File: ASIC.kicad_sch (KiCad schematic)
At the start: 69 parts, among them U10 MCP1824T-1202E/OT, U11 MCP1824T-0802E, U12 25MHz, U4 BM1370_mode1, U5 BM1370_mode1, U9 SN74AVC4T774

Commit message: start rough parts placement
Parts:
- R14: footprint (none) -> Resistor_SMD:R_0402_1005Metric; DK (none) -> 311-20.0KLRCT-ND; PARTNO (none) -> RC0402FR-0720KL
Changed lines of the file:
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@@
 			)
 		)
-		(property "Footprint" ""
+		(property "Footprint" "Resistor_SMD:R_0402_1005Metric"
 			(at 172.72 52.07 0)
 			(effects
@@
 			(at 172.72 52.07 0)
 			(effects
+				(font
+					(size 1.27 1.27)
+				)
+				(hide yes)
+			)
+		)
+		(property "PARTNO" "RC0402FR-0720KL"
+			(at 172.72 52.07 0)
+			(effects
+				(font
+					(size 1.27 1.27)
+				)
+				(hide yes)
+			)
+		)
+		(property "DK" "311-20.0KLRCT-ND"
+			(at 172.72 52.07 0)
+			(effects

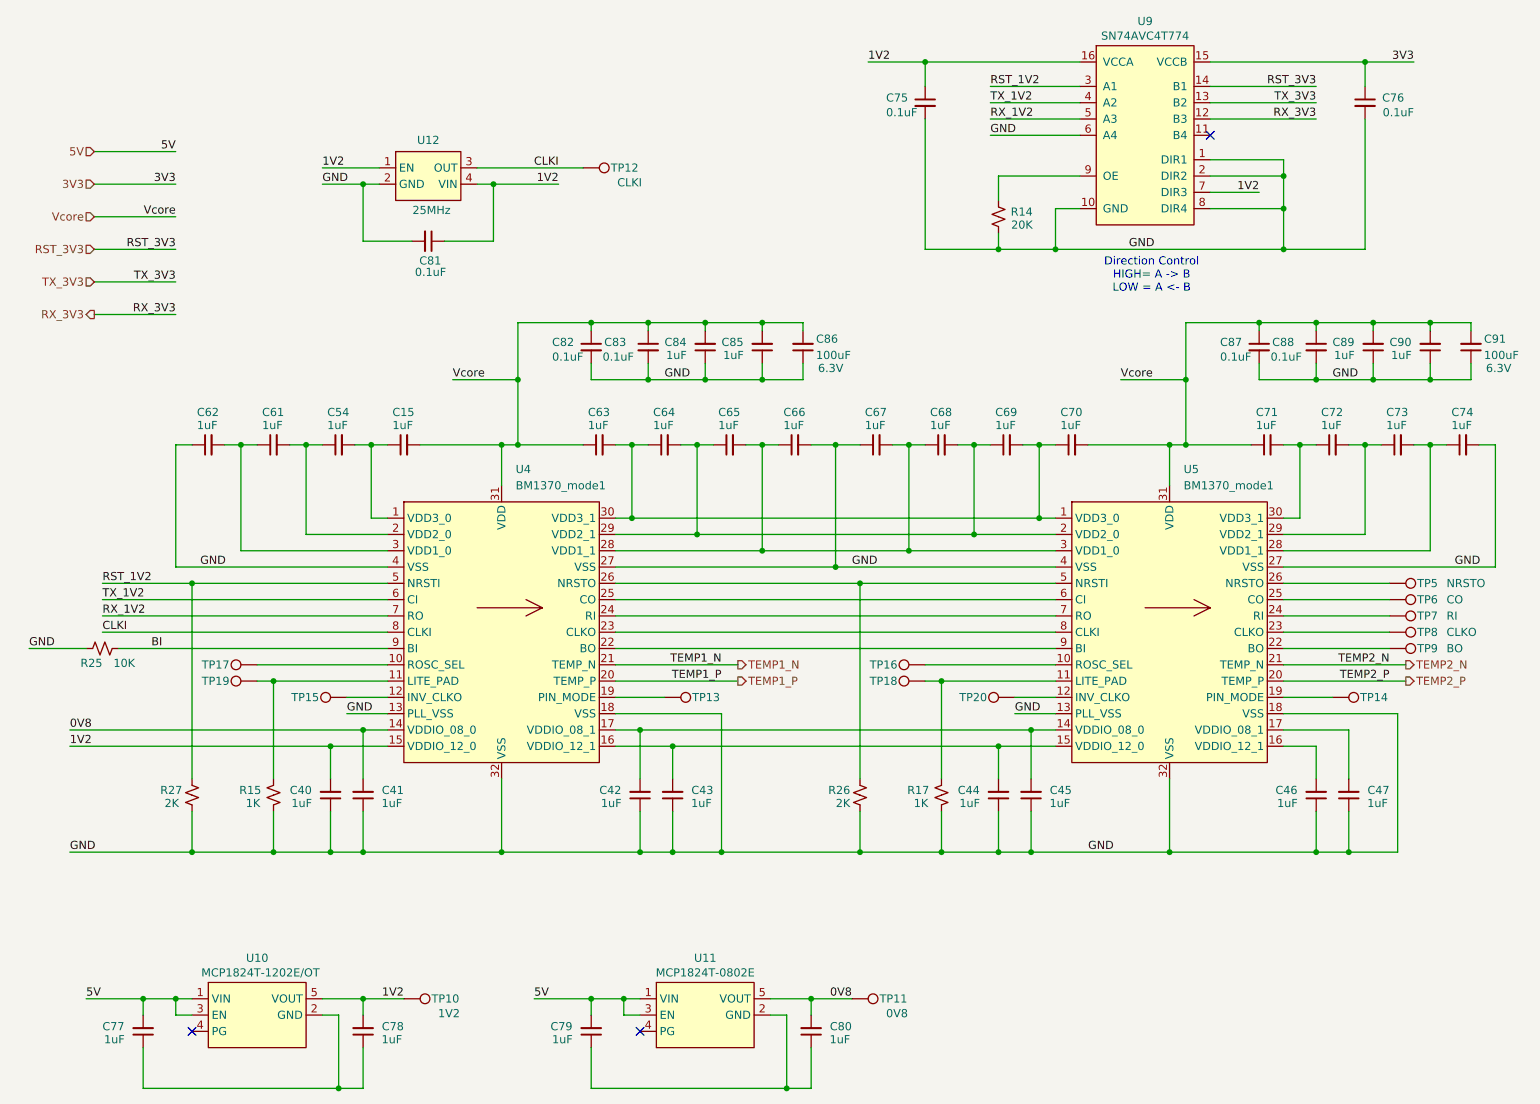
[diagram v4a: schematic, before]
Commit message: Finish assigning footprints and partnumbers
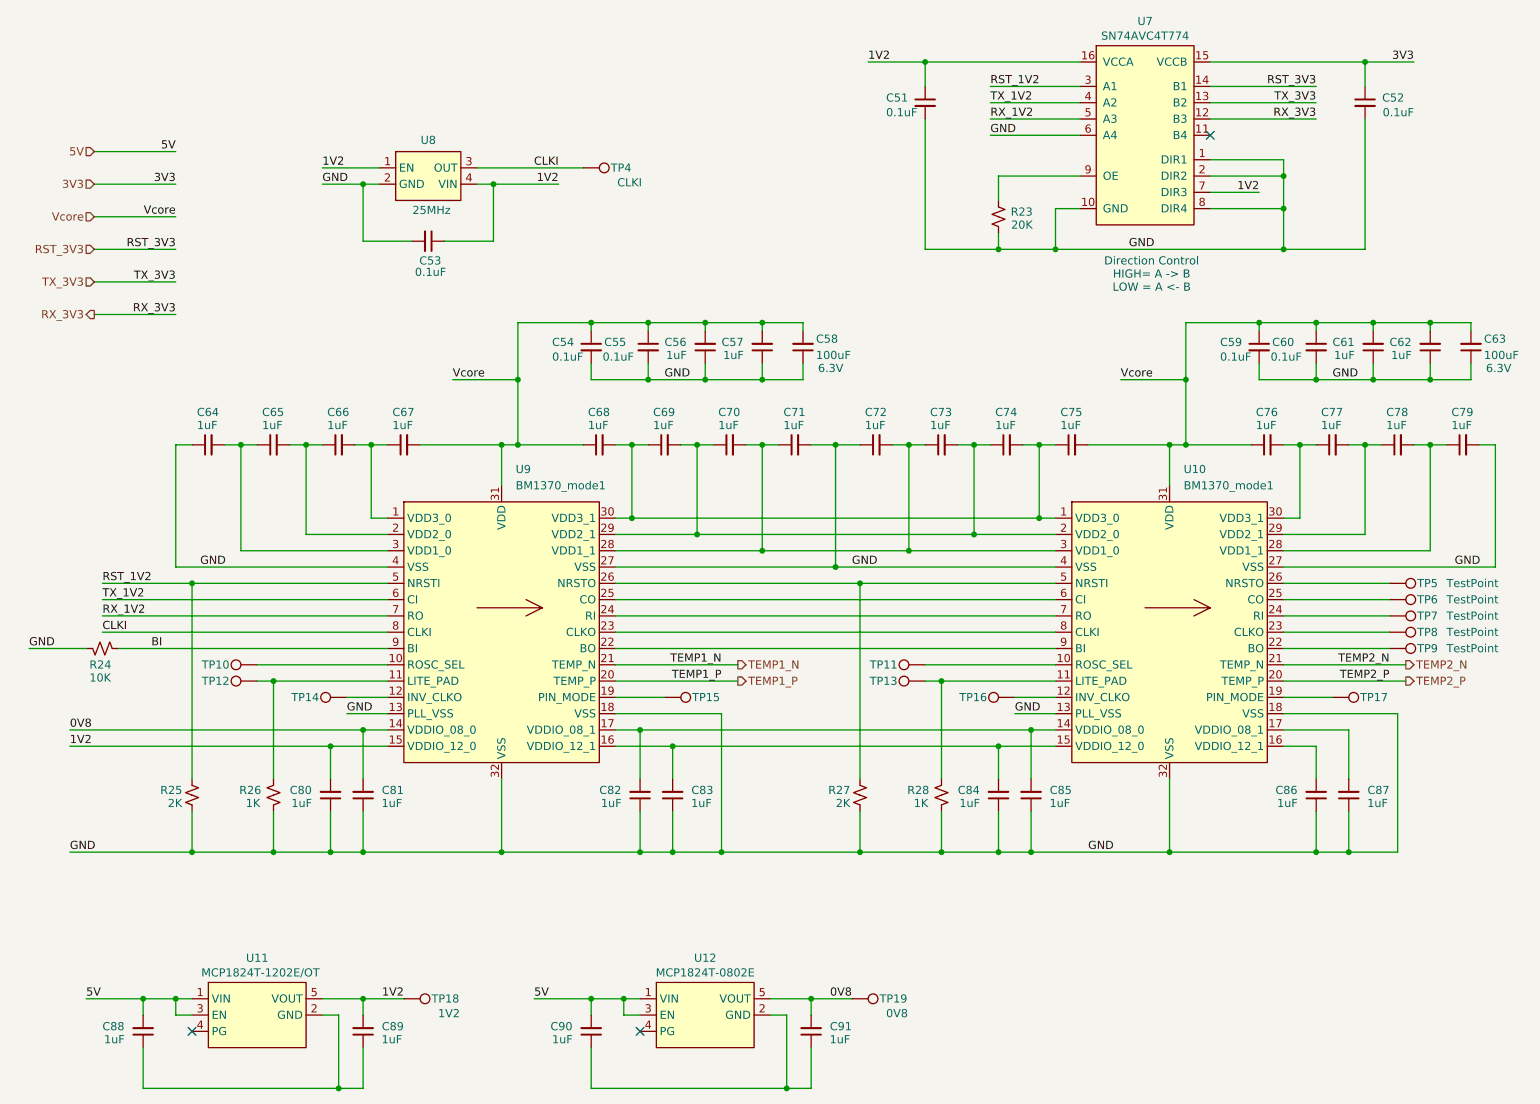
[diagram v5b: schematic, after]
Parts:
- removed R17: 1K, symbol Device:R_Small_US
- removed R27: 2K, symbol Device:R_Small_US
- added R24: 10K, Resistor_SMD:R_0402_1005Metric, symbol Device:R_Small_US
- added R28: 1K, Resistor_SMD:R_0402_1005Metric, symbol Device:R_Small_US
- R25: value 10K -> 2K; footprint (none) -> Resistor_SMD:R_0402_1005Metric; DK (none) -> YAG2303CT-ND; PARTNO (none) -> RT0402BRD072KL
- R26: renamed from R15; footprint (none) -> Resistor_SMD:R_0402_1005Metric; DK (none) -> 311-1.00KLRCT-ND; PARTNO (none) -> RC0402FR-071KL
- R27: renamed from R26; footprint (none) -> Resistor_SMD:R_0402_1005Metric; DK (none) -> YAG2303CT-ND; PARTNO (none) -> RT0402BRD072KL
- TP10: renamed from TP17; value INV_CLKO -> TestPoint; now left out of the parts list
- TP11: renamed from TP16; value INV_CLKO -> TestPoint; now left out of the parts list
- TP12: renamed from TP19; value INV_CLKO -> TestPoint; now left out of the parts list
- TP13: renamed from TP18; value INV_CLKO -> TestPoint; now left out of the parts list
- TP14: renamed from TP15; value INV_CLKO -> TestPoint; now left out of the parts list
- TP15: renamed from TP13; value PM1 -> TestPoint; now left out of the parts list
- TP16: renamed from TP20; value INV_CLKO -> TestPoint; now left out of the parts list
- TP17: renamed from TP14; value PM1 -> TestPoint; now left out of the parts list
- TP19: renamed from TP11; now left out of the parts list
- TP4: renamed from TP12; now left out of the parts list
- TP5: value NRSTO -> TestPoint; now left out of the parts list
- TP6: value CO -> TestPoint; now left out of the parts list
- TP7: value RI -> TestPoint; now left out of the parts list
- TP8: value CLKO -> TestPoint; now left out of the parts list
- TP9: value BO -> TestPoint; now left out of the parts list
- U8: renamed from U12; footprint (none) -> bitaxe:SMD3225-4P
- renumbered C75 to C51, C76 to C52, C81 to C53, C82 to C54, C83 to C55, C84 to C56, C85 to C57, C86 to C58, C87 to C59, C88 to C60, C89 to C61, C90 to C62, C91 to C63, C62 to C64, C61 to C65, C54 to C66, C15 to C67, C63 to C68, C64 to C69, C65 to C70, C66 to C71, C67 to C72, C68 to C73, C69 to C74, C70 to C75, C71 to C76, C72 to C77, C73 to C78, C74 to C79, C40 to C80, C41 to C81, C42 to C82, C43 to C83, C44 to C84, C45 to C85, C46 to C86, C47 to C87, C77 to C88, C78 to C89, C79 to C90, C80 to C91, R14 to R23, TP10 to TP18, U5 to U10, U10 to U11, U11 to U12, U9 to U7, U4 to U9
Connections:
- net BI: now also R24.1; no longer R25.2
- net GND: now also R24.2, R28.1
- net RST_1V2: now also R25.2
- net at TP13.1, U10.11 (LITE_PAD): now also R28.2

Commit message: finish creating footprints
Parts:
- TP10, TP11, TP12, TP13, TP14, TP15, TP16, TP17, TP4, TP5, TP6, TP7, TP8, TP9: footprint (none) -> TestPoint:TestPoint_Pad_D1.0mm
- TP18, TP19: footprint (none) -> TestPoint:TestPoint_Pad_D1.5mm
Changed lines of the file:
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@@
 			)
 		)
-		(property "Footprint" ""
+		(property "Footprint" "TestPoint:TestPoint_Pad_D1.0mm"
 			(at 57.15 127 0)
 			(effects
@@
 			)
 		)
-		(property "Footprint" ""
+		(property "Footprint" "TestPoint:TestPoint_Pad_D1.0mm"
 			(at 107.95 49.53 0)
 			(effects
@@
 			)
 		)
-		(property "Footprint" ""
+		(property "Footprint" "TestPoint:TestPoint_Pad_D1.0mm"
 			(at 233.68 114.3 0)
 			(effects
@@
 			)
 		)
-		(property "Footprint" ""
+		(property "Footprint" "TestPoint:TestPoint_Pad_D1.0mm"
 			(at 120.65 132.08 0)
 			(effects
@@
 			)
 		)
-		(property "Footprint" ""
+		(property "Footprint" "TestPoint:TestPoint_Pad_D1.0mm"
 			(at 233.68 116.84 0)
 			(effects
@@
 			)
 		)
-		(property "Footprint" ""
+		(property "Footprint" "TestPoint:TestPoint_Pad_D1.0mm"
 			(at 233.68 121.92 0)
 			(effects
@@
 			)
 		)
-		(property "Footprint" ""
+		(property "Footprint" "TestPoint:TestPoint_Pad_D1.0mm"
 			(at 233.68 119.38 0)
 			(effects
@@
 			)
 		)
-		(property "Footprint" ""
+		(property "Footprint" "TestPoint:TestPoint_Pad_D1.0mm"
 			(at 57.15 129.54 0)
 			(effects
@@
 			)
 		)
-		(property "Footprint" ""
+		(property "Footprint" "TestPoint:TestPoint_Pad_D1.0mm"
 			(at 161.29 127 0)
 			(effects
@@
 			)
 		)
-		(property "Footprint" ""
+		(property "Footprint" "TestPoint:TestPoint_Pad_D1.5mm"
 			(at 149.86 179.07 0)
 			(effects
@@
 			)
 		)
-		(property "Footprint" ""
+		(property "Footprint" "TestPoint:TestPoint_Pad_D1.0mm"
 			(at 224.79 132.08 0)
 			(effects
@@
 			)
 		)
-		(property "Footprint" ""
+		(property "Footprint" "TestPoint:TestPoint_Pad_D1.0mm"
 			(at 71.12 132.08 0)
 			(effects
@@
 			)
 		)
-		(property "Footprint" ""
+		(property "Footprint" "TestPoint:TestPoint_Pad_D1.0mm"
 			(at 233.68 124.46 0)
 			(effects
@@
 			)
 		)
-		(property "Footprint" ""
+		(property "Footprint" "TestPoint:TestPoint_Pad_D1.0mm"
 			(at 175.26 132.08 0)
 			(effects
@@
 			)
 		)
-		(property "Footprint" ""
+		(property "Footprint" "TestPoint:TestPoint_Pad_D1.0mm"
 			(at 161.29 129.54 0)
 			(effects
@@
 			)
 		)
-		(property "Footprint" ""
+		(property "Footprint" "TestPoint:TestPoint_Pad_D1.5mm"
 			(at 80.01 179.07 0)
 			(effects

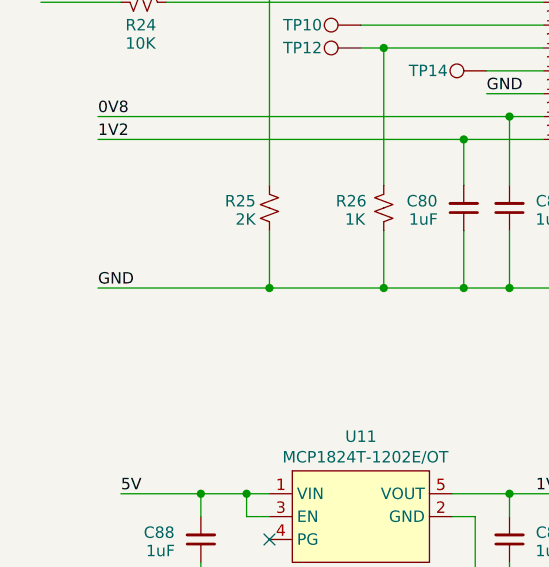
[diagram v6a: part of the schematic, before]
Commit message: more power supply routing
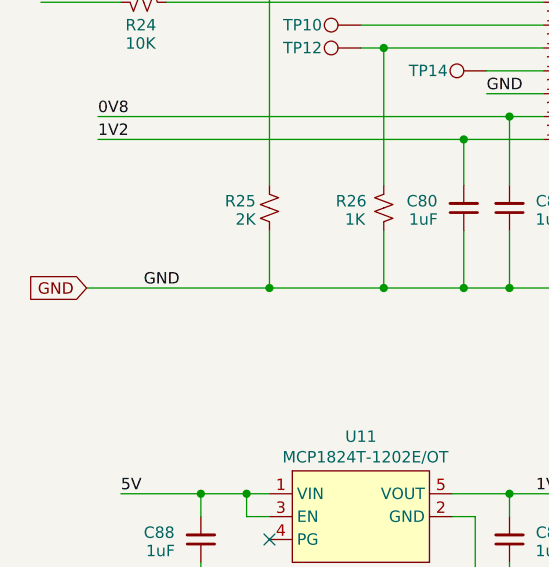
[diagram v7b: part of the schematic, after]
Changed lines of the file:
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@@
 	)
 	(junction
+		(at 46.99 151.13)
+		(diameter 0)
+		(color 0 0 0 0)
+	)
+	(junction
 		(at 199.39 151.13)
 		(diameter 0)
@@
 	)
 	(junction
-		(at 46.99 151.13)
-		(diameter 0)
-		(color 0 0 0 0)
-	)
-	(junction
 		(at 135.89 77.47)
 		(diameter 0)
@@
 	(wire
 		(pts
-			(xy 27.94 151.13) (xy 46.99 151.13)
-		)
-		(stroke
-			(width 0)
-			(type default)
-		)
-	)
-	(wire
-		(pts
 			(xy 46.99 109.22) (xy 46.99 139.7)
 		)
@@
 	(wire
 		(pts
+			(xy 26.67 151.13) (xy 46.99 151.13)
+		)
+		(stroke
+			(width 0)
+			(type default)
+		)
+	)
+	(wire
+		(pts
 			(xy 127 74.93) (xy 127 77.47)
 		)
@@
 	)
 	(label "GND"
-		(at 27.94 151.13 0)
+		(at 33.02 151.13 0)
 		(fields_autoplaced yes)
 		(effects
@@
 		)
 	)
+	(global_label "GND"
+		(shape input)
+		(at 26.67 151.13 180)
+		(fields_autoplaced yes)
+		(effects
+			(font
+				(size 1.27 1.27)
+			)
+			(justify right)
+		)
+		(property "Intersheetrefs" "${INTERSHEET_REFS}"
+			(at 19.8143 151.13 0)
+			(effects
+				(font
+					(size 1.27 1.27)
+				)
+				(justify right)
+				(hide yes)
+			)
+		)
+	)

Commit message: more parts placement
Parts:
- removed TP15, TP17: TestPoint, TestPoint:TestPoint_Pad_D1.0mm, symbol Connector:TestPoint
- removed U10, U9: BM1370_mode1, bitaxe:BM1370, symbol bitaxe:BM1370_mode1
- added U10, U9: BM1370_mode0, bitaxe:BM1370, symbol bitaxe:BM1370_mode0
- TP5: value TestPoint -> BO
- TP6: value TestPoint -> CLKO
- TP7: value TestPoint -> RO
- TP8: value TestPoint -> CO
- TP9: value TestPoint -> NRSTO
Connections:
- net 0V8: now also C82.2, C85.2, U10.14 (VDDIO_08_0), U9.17 (VDDIO_08_1); no longer C81.2
- net 1V2: now also C83.2, C84.2, U10.15 (VDDIO_12_0), U9.16 (VDDIO_12_1); no longer C80.2
- net BI: now also U10.26 (BI)
- net CLKI: now also U10.25 (CLKI)
- net GND: now also U10.13 (PLL_VSS), U10.18 (VSS), U10.19 (PIN_MODE), U10.27 (VSS), U10.32 (VSS), U10.4 (VSS), U9.13 (PLL_VSS), U9.18 (VSS), U9.19 (PIN_MODE), U9.27 (VSS), U9.32 (VSS), U9.4 (VSS)
- net RST_1V2: now also U10.22 (NRSTI)
- net RX_1V2: now also U10.24 (RI)
- net TEMP1_N: now also U9.21 (TEMP_N)
- net TEMP1_P: now also U9.20 (TEMP_P)
- net TEMP2_N: now also U10.21 (TEMP_N)
- net TEMP2_P: now also U10.20 (TEMP_P)
- net TX_1V2: now also U10.23 (CI)
- net Vcore: now also U10.31 (VDD), U9.31 (VDD)
- net at TP10.1: now also U9.10 (ROSC_SEL)
- net at R26.2, TP12.1: now also U9.11 (LITE_PAD)
- net at C70.2, C71.1, C72.2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: now also U10.3 (VDD1_0), U9.28 (VDD1_1)
- net at C69.2, C70.1, C73.2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: now also U10.2 (VDD2_0), U9.29 (VDD2_1)
- net at C78.2, C79.1: now also U10.28 (VDD1_1)
- net at TP5.1: now also U9.5 (BO)
- net at C68.2, C69.1, C74.2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: now also U10.1 (VDD3_0), U9.30 (VDD3_1)
- net at TP6.1: now also U9.6 (CLKO)
- net at C64.2, C65.1: now also U9.3 (VDD1_0)
- net at C65.2, C66.1: now also U9.2 (VDD2_0)
- net at R28.2, TP13.1: now also U10.11 (LITE_PAD)
- net at TP11.1: now also U10.10 (ROSC_SEL)
- net at TP16.1: now also U10.12 (INV_CLKO)
- net 1V2_2: now reaches C86.2
- net 1V2_2: now also U10.16 (VDDIO_12_1)
- net 0V8_2: now reaches C87.2
- net 0V8_2: now also U10.17 (VDDIO_08_1)
- net at TP9.1: now also U9.9 (NRSTO)
- net at TP8.1: now also U9.8 (CO)
- net at TP7.1: now also U9.7 (RO)
- net at C77.2, C78.1: now also U10.29 (VDD2_1)
- net at C76.2, C77.1: now also U10.30 (VDD3_1)
- net at R27.2: now also U10.9 (NRSTO), U9.22 (NRSTI)
- net at C66.2, C67.1: now also U9.1 (VDD3_0)
- net at TP14.1: now also U9.12 (INV_CLKO)
- new net: U10.8 (CO), U9.23 (CI)
- new net: U10.7 (RO), U9.24 (RI)
- new net: U10.6 (CLKO), U9.25 (CLKI)
- new net: U10.5 (BO), U9.26 (BI)
- new net 0V8_1: C80.2, U9.14 (VDDIO_08_0)
- new net 1V2_1: C81.2, U9.15 (VDDIO_12_0)
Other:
- moved on the sheet: C80, C81, C86, C87, R26, R27, TP10, TP12, TP5, TP6, TP7, TP8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
